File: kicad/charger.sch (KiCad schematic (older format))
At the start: 24 parts, among them IC4 BQ24079RGTR, J14 Ammeter_Jumper, U6 SPX3819M5-L, U7 BQ27421YZFR-G1A, U8 SN74LV00ARGYR

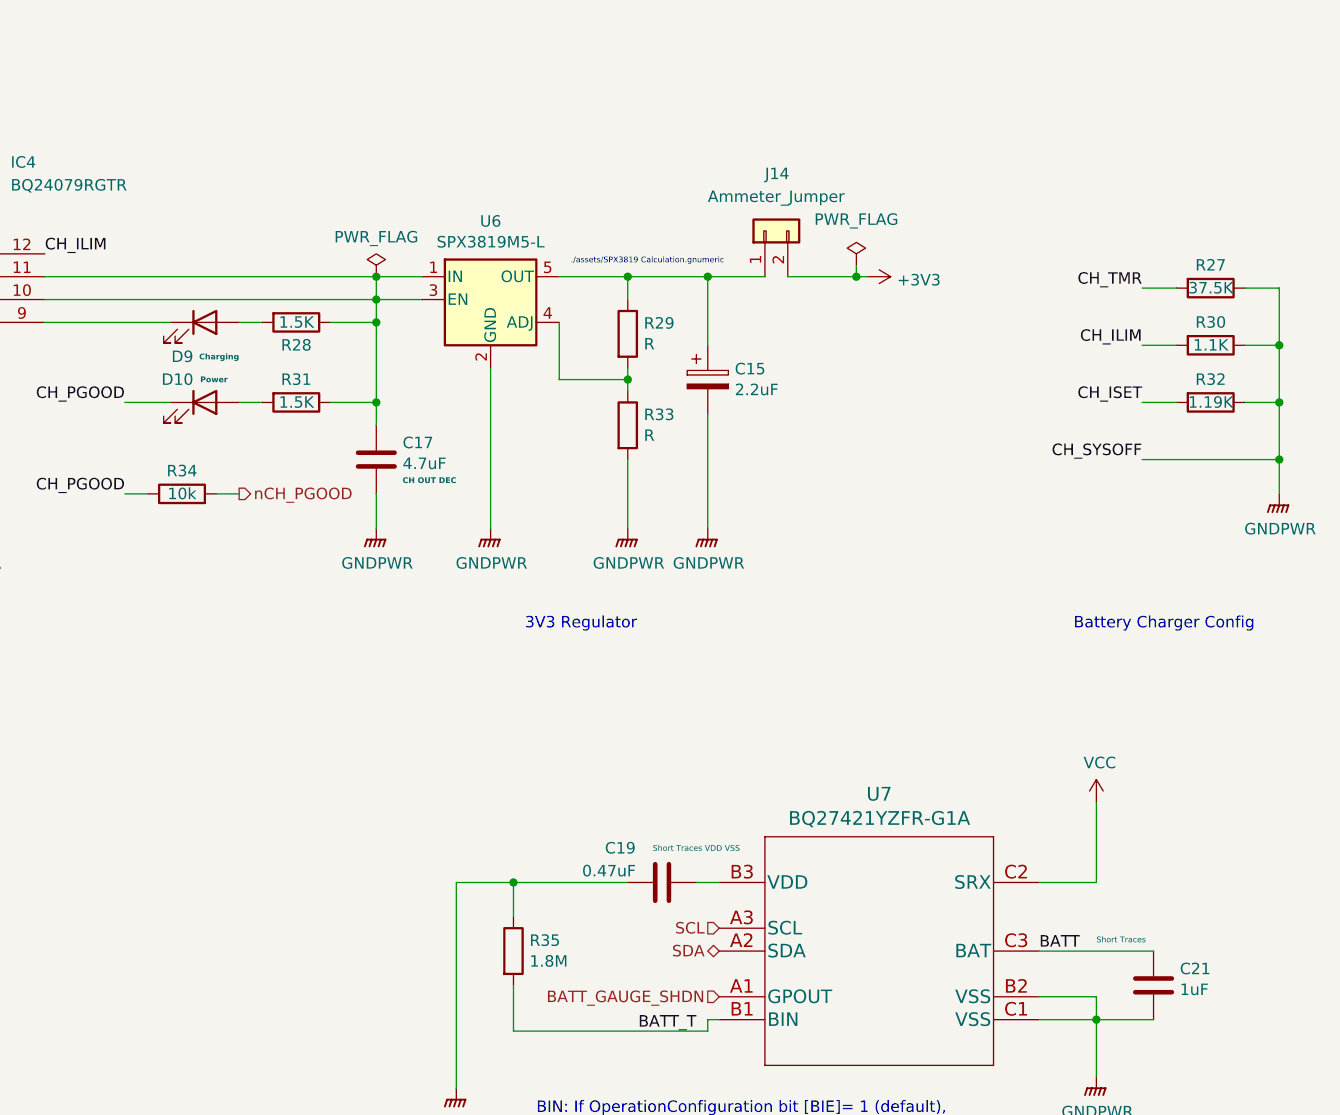
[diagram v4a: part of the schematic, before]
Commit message: Mapped footprints, PCB in progress
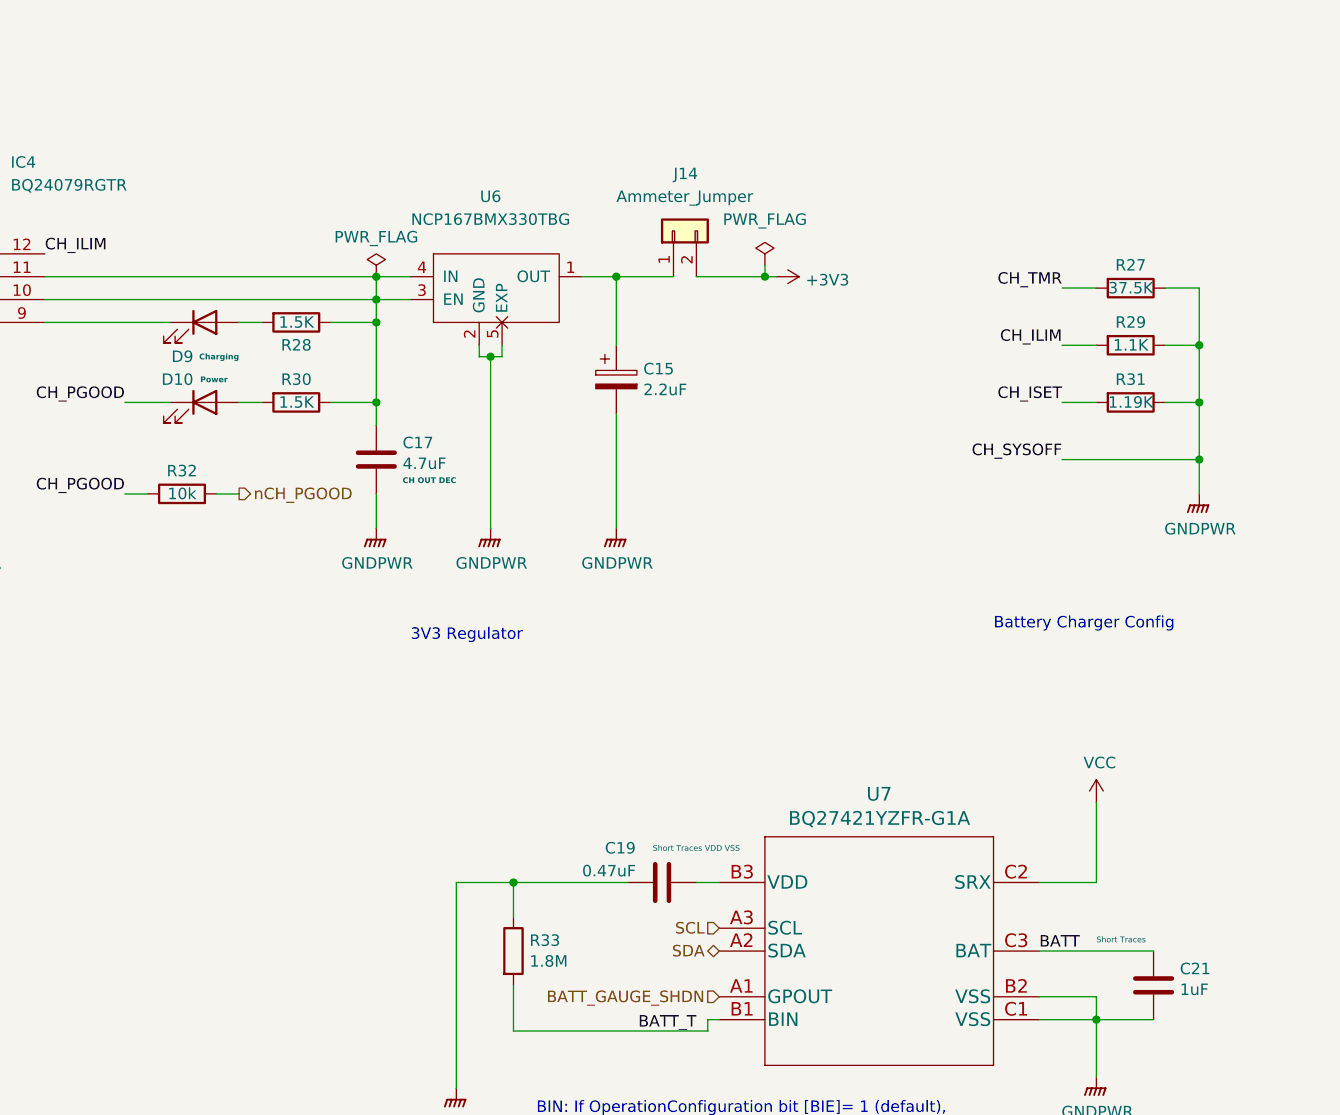
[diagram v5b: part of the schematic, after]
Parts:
- removed R29, R33: R, Resistor_SMD:R_0805_2012Metric, symbol Device:R
- removed U6: SPX3819M5-L, Package_TO_SOT_SMD:SOT-23-5, symbol Regulator_Linear:SPX3819M5-L
- added U6: NCP167BMX330TBG, Parts:REG_NCP167BMX330TBG, symbol Parts:NCP167BMX330TBG
- renumbered R30 to R29, R31 to R30, R32 to R31, R34 to R32, R35 to R33
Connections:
- net GNDPWR: now also U6.2 (GND), U6.5 (EXP)
- net at C17.1, IC4.10 (OUT_1), IC4.11 (OUT_2)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: now also U6.3 (EN), U6.4 (IN)
- net at C15.1, J14.1 (Pin_1): now also U6.1 (OUT)
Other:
- note removed: "./assets/SPX3819 Calculation.gnumeric"
- moved on the sheet: C15, J14, R27, R29, R31
